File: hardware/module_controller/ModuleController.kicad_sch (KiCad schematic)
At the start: 23 parts, among them J1 JST05_StepperMotor, J6 Conn_02x08_Top_Bottom, U1 ULN2003, U2 A1101ELHL, U3 SN75176AP, U4 ATmega8A-A, Y1 16MHz

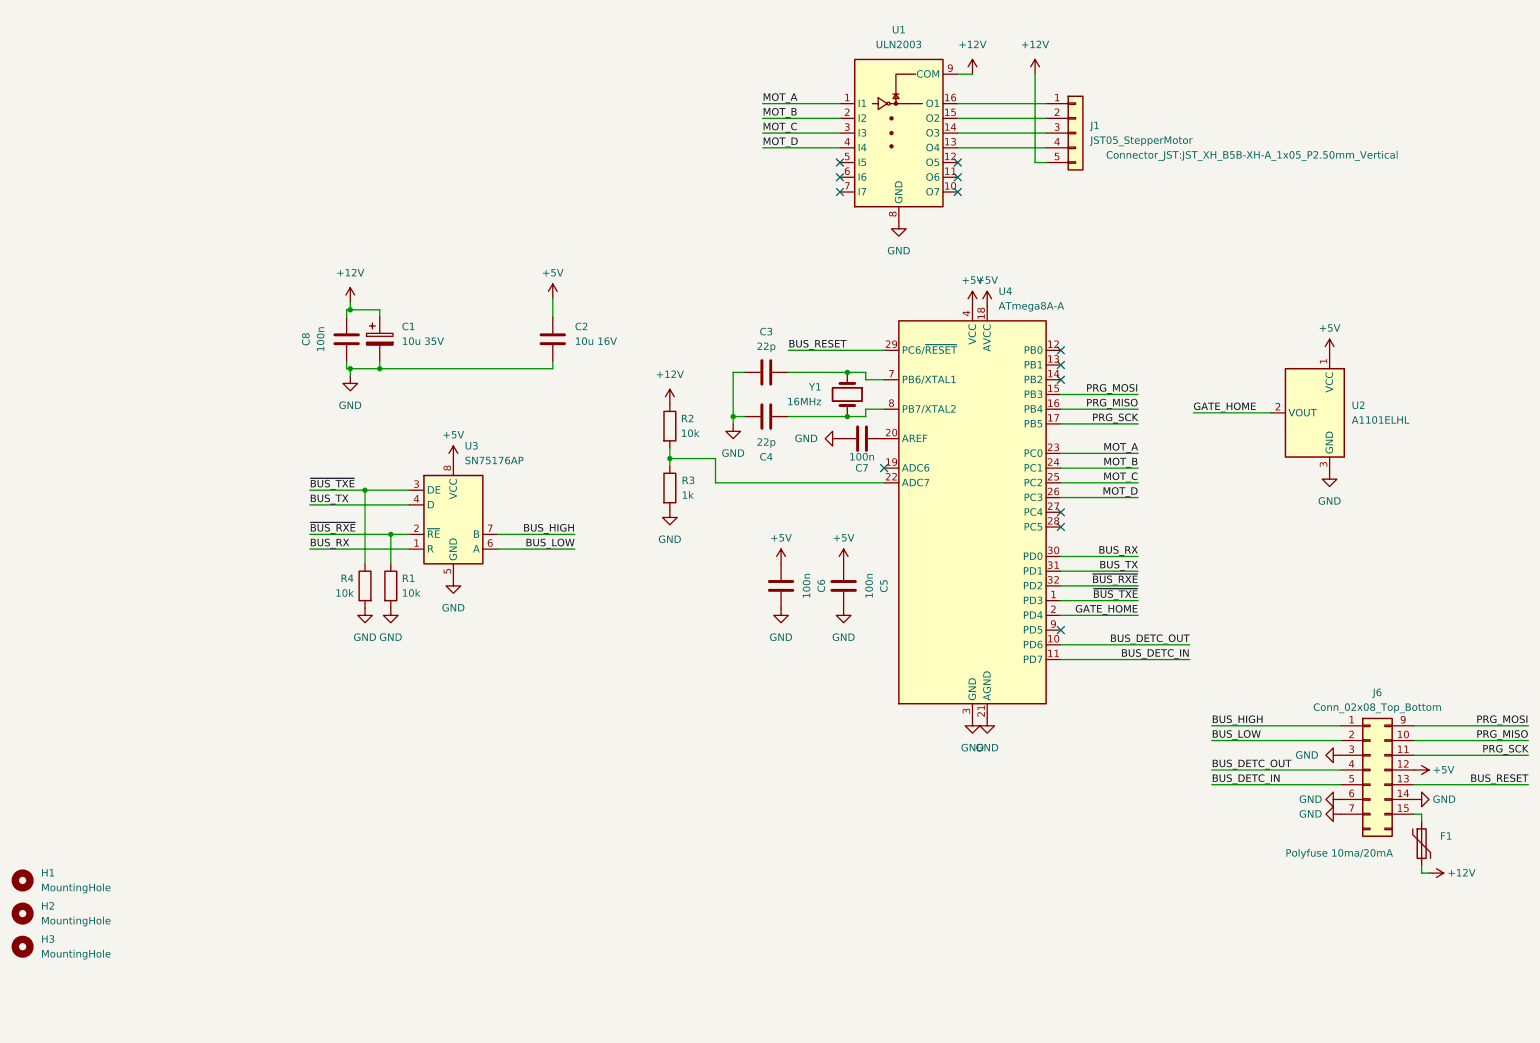
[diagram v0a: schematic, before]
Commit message: Refactor schematics
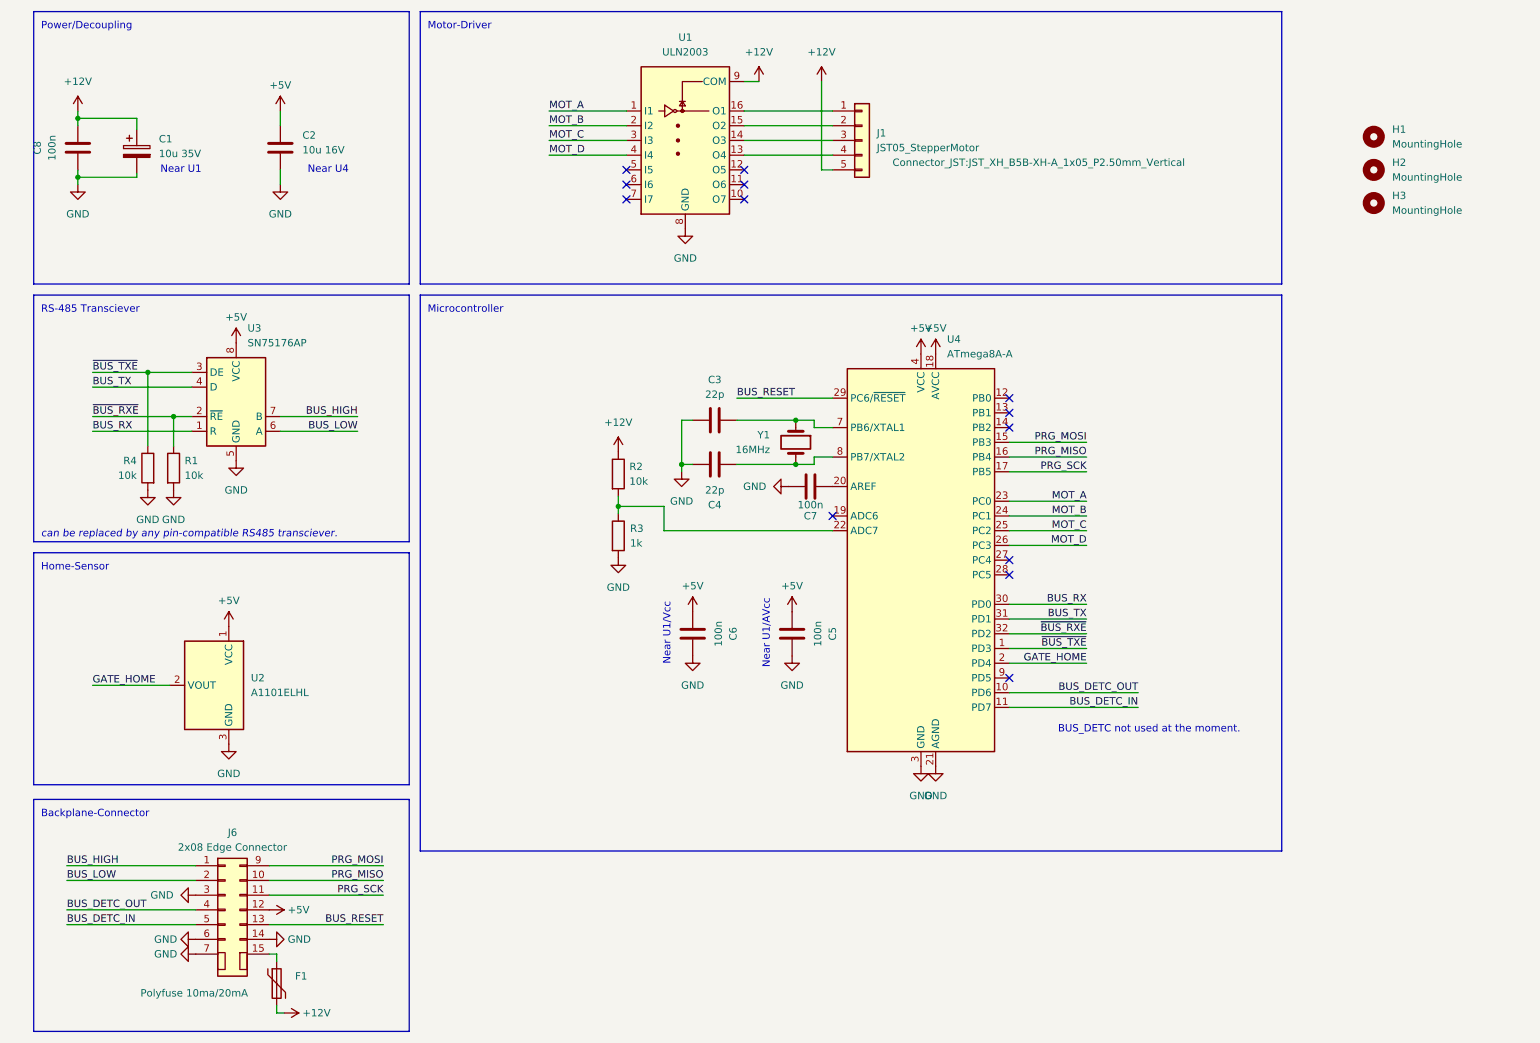
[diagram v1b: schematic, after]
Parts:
- J6: value Conn_02x08_Top_Bottom -> 2x08 Edge Connector
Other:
- note added: "BUS_DETC not used at the moment."
- note added: "Backplane-Connector"
- note added: "Home-Sensor"
- note added: "Microcontroller"
- note added: "Motor-Driver"
- note added: "Near U1"
- note added: "Near U1/AVcc"
- note added: "Near U1/Vcc"
- note added: "Near U4"
- note added: "Power/Decoupling"
- note added: "RS-485 Transciever"
- note added: "can be replaced by any pin-compatible RS485 transciever."
- company: (none) -> Dennis Gunia www.dennisgunia.de
- title: (none) -> Split-Flap Module Controller 
- moved on the sheet: C1, C2, C3, C4, C5, C6, C7, C8, F1, H1, H2, H3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
